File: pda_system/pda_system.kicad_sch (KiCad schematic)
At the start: 17 parts, among them J1 Screw_Terminal_01x04, U1 STM32F103C8Tx, U2 SN65HVD230, U3 MP2303ADP, Y1 8Mhz

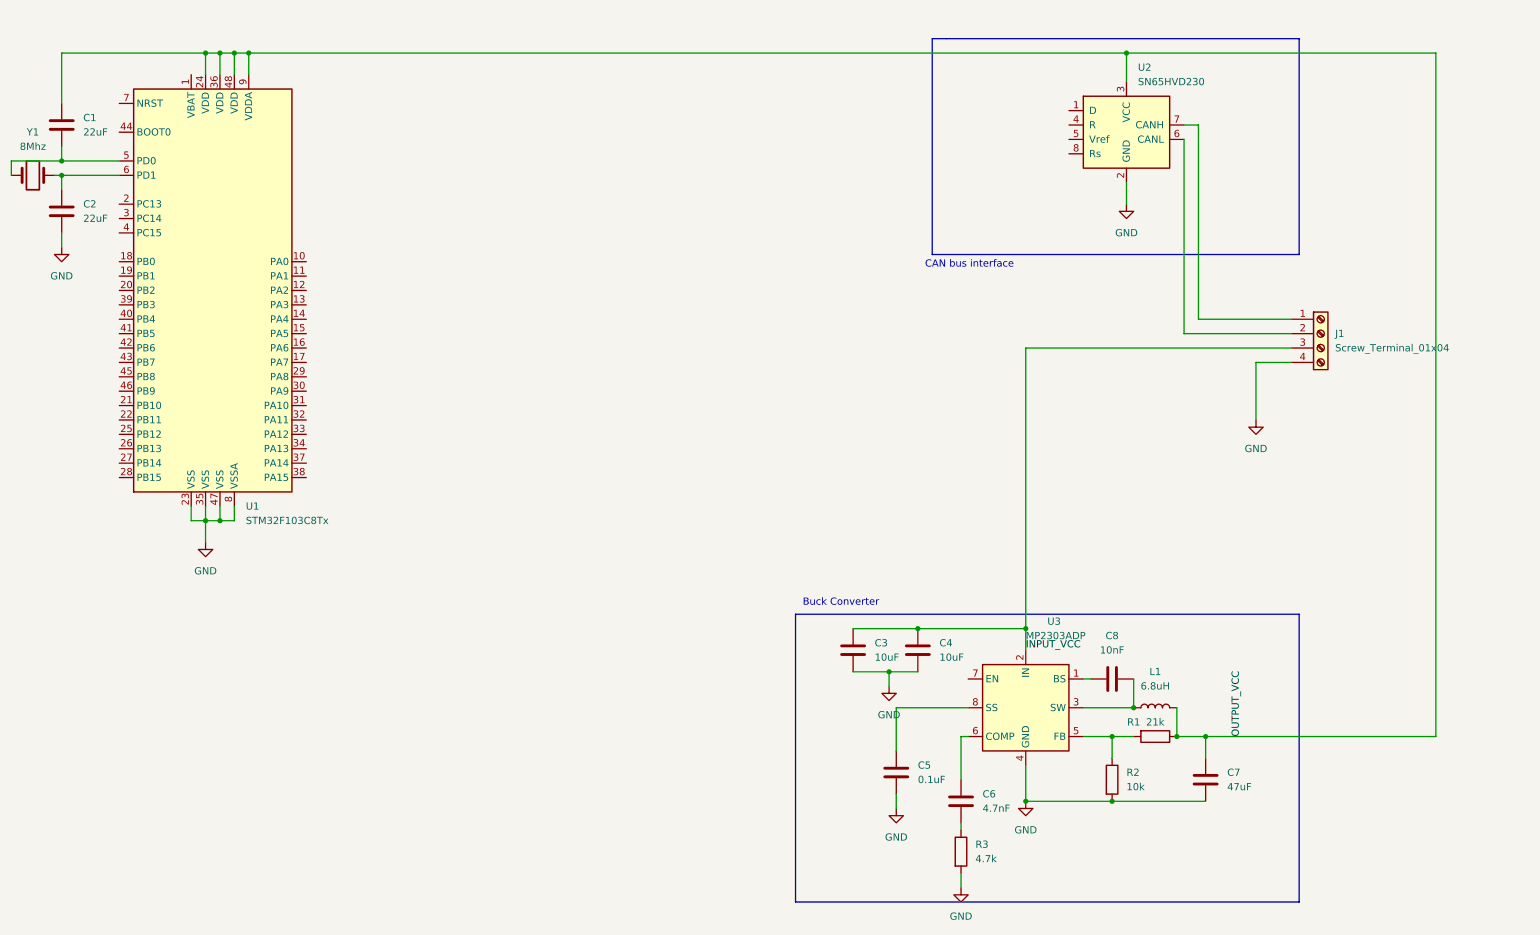
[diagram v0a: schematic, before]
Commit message: updated the main schematic to include heiarchical sheet for the mini360 power supply
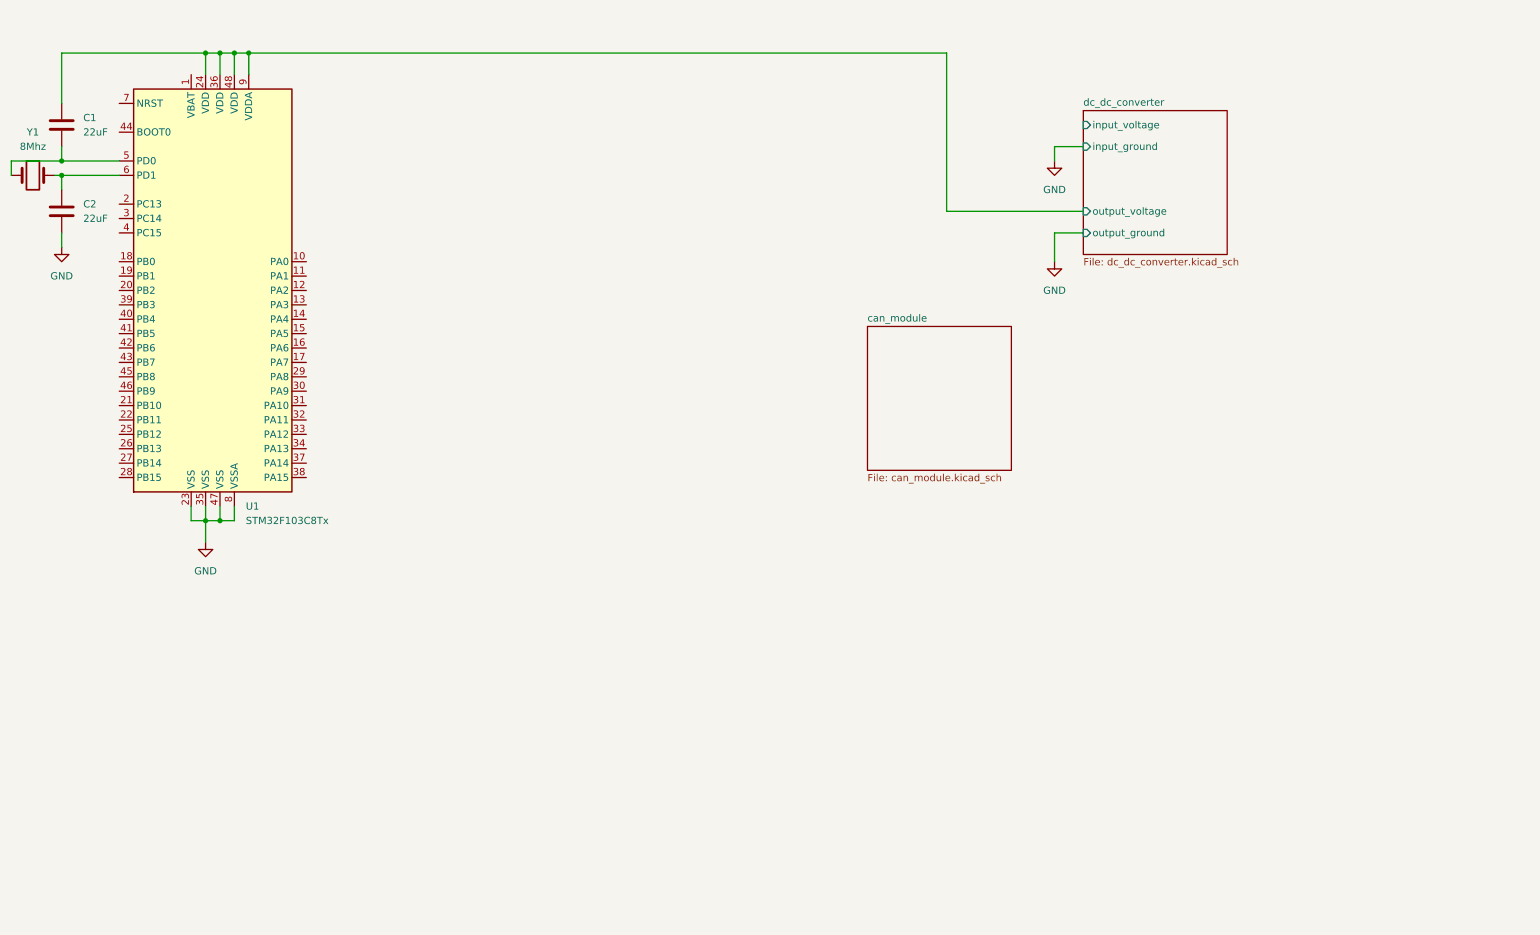
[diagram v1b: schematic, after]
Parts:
- removed C3, C4: 10uF, symbol Device:C
- removed C5: 0.1uF, symbol Device:C
- removed C6: 4.7nF, symbol Device:C
- removed C7: 47uF, symbol Device:C
- removed C8: 10nF, symbol Device:C
- removed J1: Screw_Terminal_01x04, symbol Connector:Screw_Terminal_01x04
- removed L1: 6.8uH, symbol Device:L
- removed R1: 21k, symbol Device:R
- removed R2: 10k, symbol Device:R
- removed R3: 4.7k, symbol Device:R
- removed U2: SN65HVD230, Package_SO:SOIC-8_3.9x4.9mm_P1.27mm, symbol Interface_CAN_LIN:SN65HVD230
- removed U3: MP2303ADP, Package_DIP:DIP-8_W7.62mm, symbol Regulator_Switching:MP2303ADP
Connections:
- net OUTPUT_VCC renamed dc_dc_converter/output_voltage
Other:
- added sheet can_module (can_module.kicad_sch)
- added sheet dc_dc_converter (dc_dc_converter.kicad_sch)
- note removed: "Buck Converter"
- note removed: "CAN bus interface"

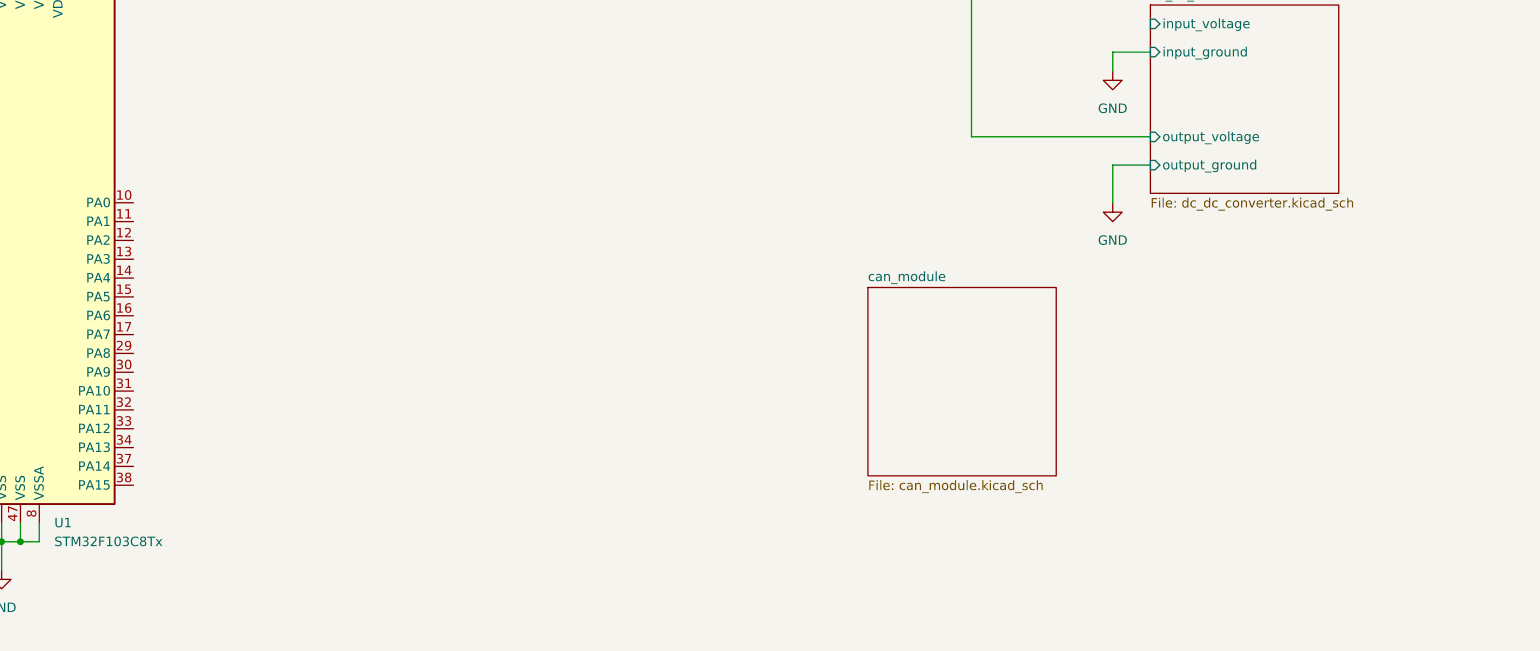
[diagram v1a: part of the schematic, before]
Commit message: updated to use heiarchical sheets for the main schematic
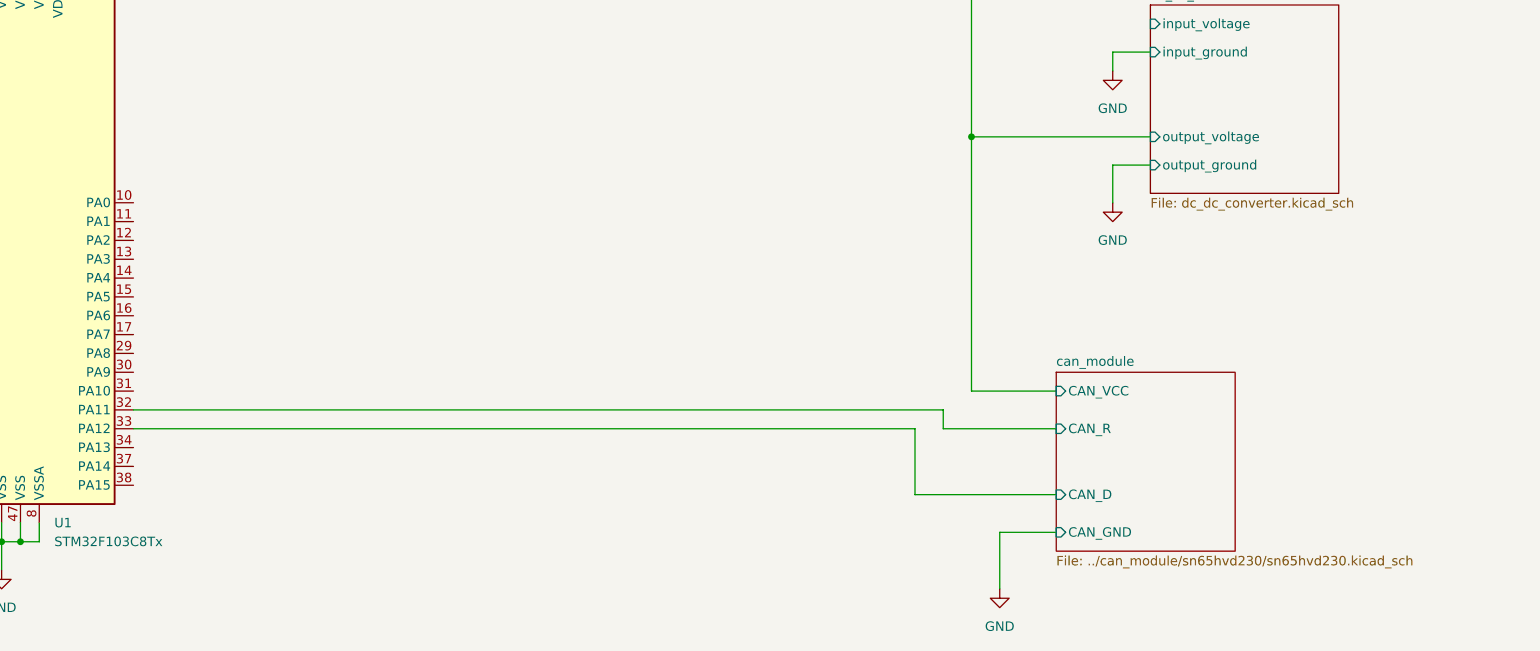
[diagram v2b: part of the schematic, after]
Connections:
- net can_module/CAN_R: now reaches U1.32 (PA11)
- net can_module/CAN_D: now reaches U1.33 (PA12)
- net dc_dc_converter/output_voltage renamed can_module/CAN_VCC
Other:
- sheet can_module: file can_module.kicad_sch -> ../can_module/sn65hvd230/sn65hvd230.kicad_sch
- sheet can_module ports: added CAN_D, CAN_GND, CAN_R, CAN_VCC; removed none
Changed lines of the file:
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@@
   (junction (at 35.56 36.83) (diameter 0) (color 0 0 0 0)
   )
+  (junction (at 191.77 43.18) (diameter 0) (color 0 0 0 0)
+  )
   (junction (at 60.96 97.79) (diameter 0) (color 0 0 0 0)
   )
@@
     (stroke (width 0) (type default) (color 0 0 0 0))
   )
+  (wire (pts (xy 203.2 77.47) (xy 191.77 77.47))
+    (stroke (width 0) (type default) (color 0 0 0 0))
+  )
   (wire (pts (xy 60.96 95.25) (xy 60.96 97.79))
     (stroke (width 0) (type default) (color 0 0 0 0))
@@
     (stroke (width 0) (type default) (color 0 0 0 0))
   )
+  (wire (pts (xy 187.96 80.01) (xy 187.96 82.55))
+    (stroke (width 0) (type default) (color 0 0 0 0))
+  )
+  (wire (pts (xy 78.74 80.01) (xy 187.96 80.01))
+    (stroke (width 0) (type default) (color 0 0 0 0))
+  )
+  (wire (pts (xy 191.77 77.47) (xy 191.77 43.18))
+    (stroke (width 0) (type default) (color 0 0 0 0))
+  )
+  (wire (pts (xy 195.58 96.52) (xy 195.58 104.14))
+    (stroke (width 0) (type default) (color 0 0 0 0))
+  )
+  (wire (pts (xy 203.2 96.52) (xy 195.58 96.52))
+    (stroke (width 0) (type default) (color 0 0 0 0))
+  )
   (wire (pts (xy 35.56 36.83) (xy 45.72 36.83))
     (stroke (width 0) (type default) (color 0 0 0 0))
   )
+  (wire (pts (xy 187.96 82.55) (xy 203.2 82.55))
+    (stroke (width 0) (type default) (color 0 0 0 0))
+  )
   (wire (pts (xy 35.56 15.24) (xy 60.96 15.24))
     (stroke (width 0) (type default) (color 0 0 0 0))
@@
     (stroke (width 0) (type default) (color 0 0 0 0))
   )
+  (wire (pts (xy 78.74 82.55) (xy 184.15 82.55))
+    (stroke (width 0) (type default) (color 0 0 0 0))
+  )
   (wire (pts (xy 35.56 46.99) (xy 35.56 49.53))
     (stroke (width 0) (type default) (color 0 0 0 0))
@@
     (stroke (width 0) (type default) (color 0 0 0 0))
   )
+  (wire (pts (xy 184.15 91.44) (xy 203.2 91.44))
+    (stroke (width 0) (type default) (color 0 0 0 0))
+  )
   (wire (pts (xy 66.04 97.79) (xy 63.5 97.79))
     (stroke (width 0) (type default) (color 0 0 0 0))
@@
   )
   (wire (pts (xy 68.58 19.05) (xy 68.58 15.24))
+    (stroke (width 0) (type default) (color 0 0 0 0))
+  )
+  (wire (pts (xy 184.15 82.55) (xy 184.15 91.44))
     (stroke (width 0) (type default) (color 0 0 0 0))
   )
@@
     (pin "1")
   )
+  (symbol (lib_id "power:GND") (at 195.58 104.14 0) (unit 1)
+    (in_bom yes) (on_board yes) (fields_autoplaced)
+    (property "Reference" "#PWR?" (id 0) (at 195.58 110.49 0)
+      (effects (font (size 1.27 1.27)) hide)
+    )
+    (property "Value" "GND" (id 1) (at 195.58 109.22 0))
+    (property "Footprint" "" (id 2) (at 195.58 104.14 0)
+      (effects (font (size 1.27 1.27)) hide)
+    )
+    (property "Datasheet" "" (id 3) (at 195.58 104.14 0)
+      (effects (font (size 1.27 1.27)) hide)
+    )
+    (pin "1")
+  )
   (symbol (lib_id "Device:Crystal") (at 30.48 36.83 0) (unit 1)
     (in_bom yes) (on_board yes) (fields_autoplaced)
@@
     (pin "2")
   )
-  (sheet (at 177.8 63.5) (size 25.4 25.4) (fields_autoplaced)
+  (sheet (at 203.2 74.93) (size 24.13 24.13) (fields_autoplaced)
     (stroke (width 0.1524) (type solid) (color 0 0 0 0))
     (fill (color 0 0 0 0.0000))
-    (property "Sheet name" "can_module" (id 0) (at 177.8 62.7884 0)
+    (property "Sheet name" "can_module" (id 0) (at 203.2 74.2184 0)
       (effects (font (size 1.27 1.27)) (justify left bottom))
     )
-    (property "Sheet file" "can_module.kicad_sch" (id 1) (at 177.8 89.4846 0)
+    (property "Sheet file" "../can_module/sn65hvd230/sn65hvd230.kicad_sch" (id 1) (at 203.2 99.6446 0)
       (effects (font (size 1.27 1.27)) (justify left top))
+    )
+    (pin "CAN_GND" input (at 203.2 96.52 180)
+      (effects (font (size 1.27 1.27)) (justify left))
+    )
+    (pin "CAN_VCC" input (at 203.2 77.47 180)
+      (effects (font (size 1.27 1.27)) (justify left))
+    )
+    (pin "CAN_R" input (at 203.2 82.55 180)
+      (effects (font (size 1.27 1.27)) (justify left))
+    )
+    (pin "CAN_D" input (at 203.2 91.44 180)
+      (effects (font (size 1.27 1.27)) (justify left))
     )
   )
@@
     (path "/" (page "1"))
     (path "/5ffeb525-fdbf-4755-b592-8d08c6d7cfa4" (page "2"))
-    (path "/5c858850-a41f-49c6-9b99-446d78ce9910" (page "3"))
+    (path "/4a734e8c-369c-4bb8-b786-a974b034cd31" (page "3"))
   )
   (symbol_instances
+    (path "/4a734e8c-369c-4bb8-b786-a974b034cd31/1c3627f9-1535-4f55-a7b1-ecb389a7d580"
+      (reference "#PWR01") (unit 1) (value "GND") (footprint "")
+    )
     (path "/5ffeb525-fdbf-4755-b592-8d08c6d7cfa4/c382b12a-2eb6-4570-9871-f5e05861e641"
       (reference "#PWR0101") (unit 1) (value "GND") (footprint "")
@@
       (reference "#PWR?") (unit 1) (value "GND") (footprint "")
     )
+    (path "/710593bb-ca6d-4efb-a8f4-aef0511d0cb8"
+      (reference "#PWR?") (unit 1) (value "GND") (footprint "")
+    )
     (path "/b46e5ed6-9b2f-46ad-8a6e-2c61aa21e8ae"
       (reference "#PWR?") (unit 1) (value "GND") (footprint "")
@@
       (reference "C?") (unit 1) (value "0.1uF") (footprint "")
     )
+    (path "/4a734e8c-369c-4bb8-b786-a974b034cd31/4f4b751d-4323-43d3-b6b1-ce0d095a67bf"
+      (reference "J1") (unit 1) (value "Conn_01x04") (footprint "Connector_PinHeader_2.54mm:PinHeader_1x04_P2.54mm_Horizontal")
+    )
+    (path "/4a734e8c-369c-4bb8-b786-a974b034cd31/137bca6b-874f-43e3-b202-f2b57e235d86"
+      (reference "J2") (unit 1) (value "Conn_01x02") (footprint "TerminalBlock:TerminalBlock_bornier-2_P5.08mm")
+    )
     (path "/5ffeb525-fdbf-4755-b592-8d08c6d7cfa4/414dda4b-de85-4ea6-8155-fd9c895f4036"
       (reference "J?") (unit 1) (value "GND") (footprint "")
@@
       (reference "L?") (unit 1) (value "2uH") (footprint "")
     )
+    (path "/4a734e8c-369c-4bb8-b786-a974b034cd31/55a6bd68-8a04-49f4-9ca3-4a38d1abe34a"
+      (reference "R1") (unit 1) (value "10k") (footprint "Resistor_THT:R_Axial_DIN0204_L3.6mm_D1.6mm_P5.08mm_Horizontal")
+    )
+    (path "/4a734e8c-369c-4bb8-b786-a974b034cd31/a9d01d06-d5b2-4c3b-b0da-a332b41094f8"
+      (reference "R2") (unit 1) (value "120") (footprint "Resistor_THT:R_Axial_DIN0204_L3.6mm_D1.6mm_P5.08mm_Horizontal")
+    )
     (path "/5ffeb525-fdbf-4755-b592-8d08c6d7cfa4/04b4bf19-e359-4911-80d9-8298e073d5e3"
       (reference "R?") (unit 1) (value "100k") (footprint "")
@@
       (reference "RV?") (unit 1) (value "220k") (footprint "")
     )
+    (path "/4a734e8c-369c-4bb8-b786-a974b034cd31/0f54db53-a272-4955-88fb-d7ab00657bb0"
+      (reference "U1") (unit 1) (value "SN65HVD230") (footprint "Package_SO:SOIC-8_3.9x4.9mm_P1.27mm")
+    )
     (path "/240c10af-51b5-420e-a6f4-a2c8f5db1db5"
